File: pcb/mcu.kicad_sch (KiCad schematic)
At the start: 6 parts, among them U5 STM32G0B1RET6

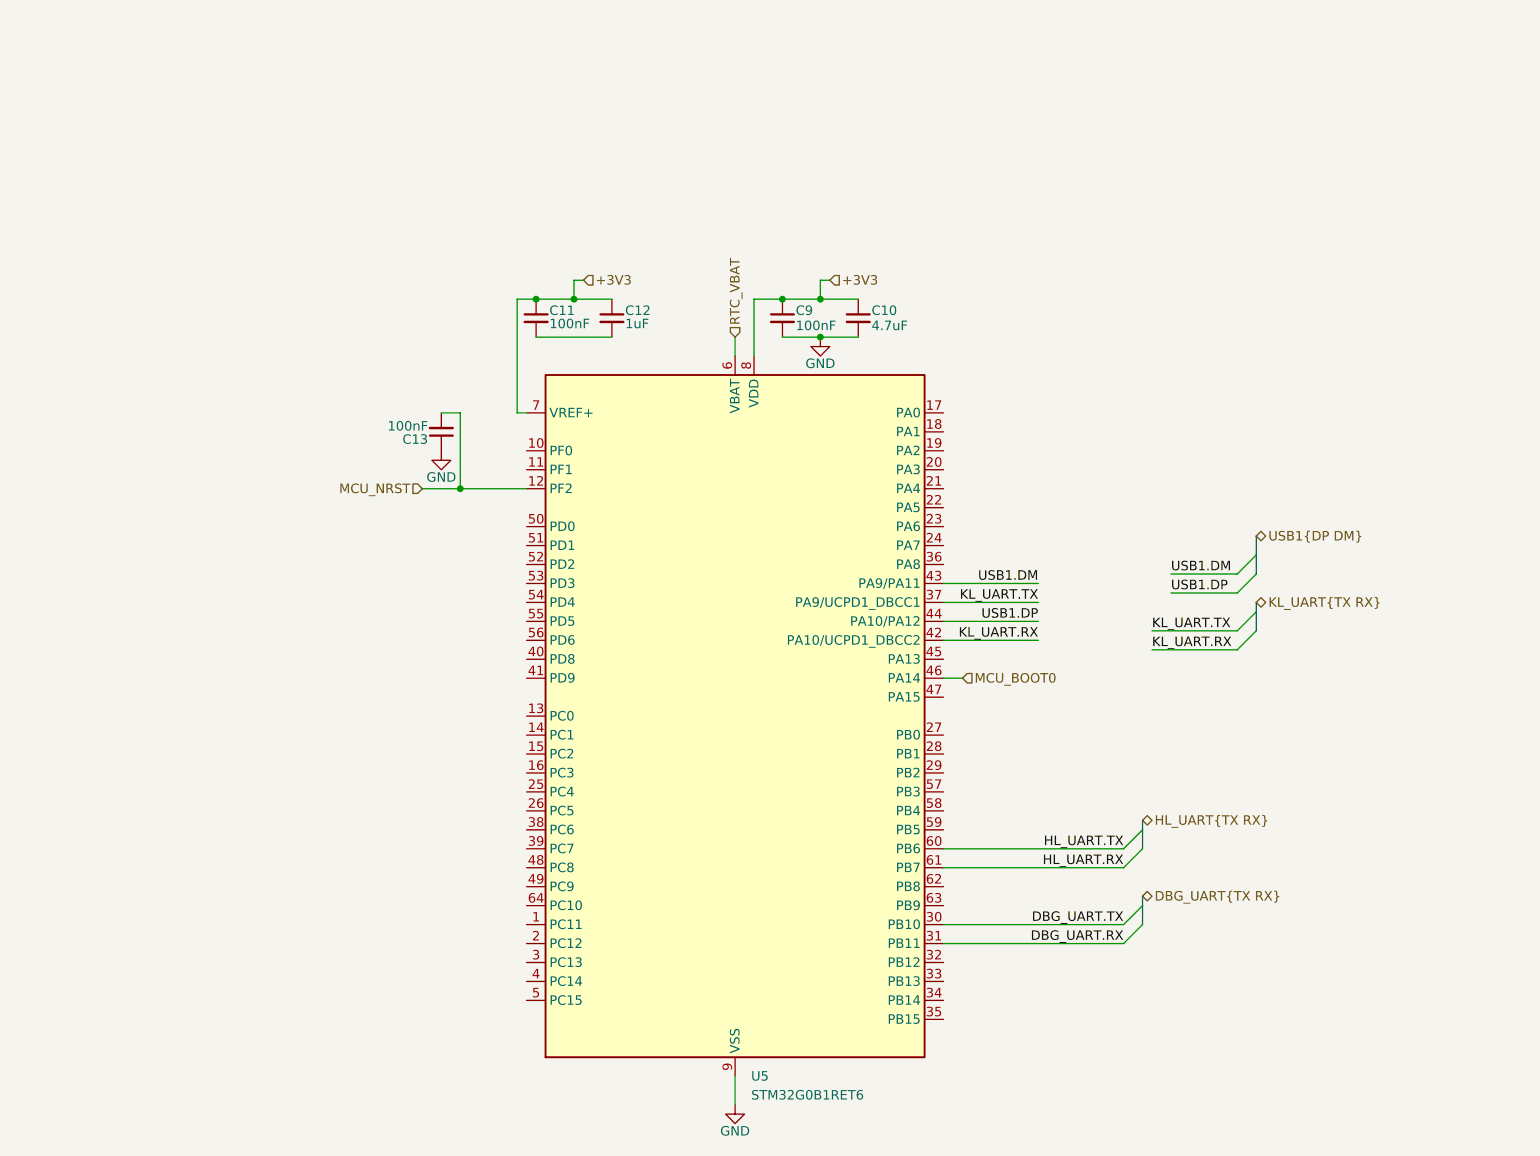
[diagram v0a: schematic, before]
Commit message: pcb gitignore update, netting and mcu pinning
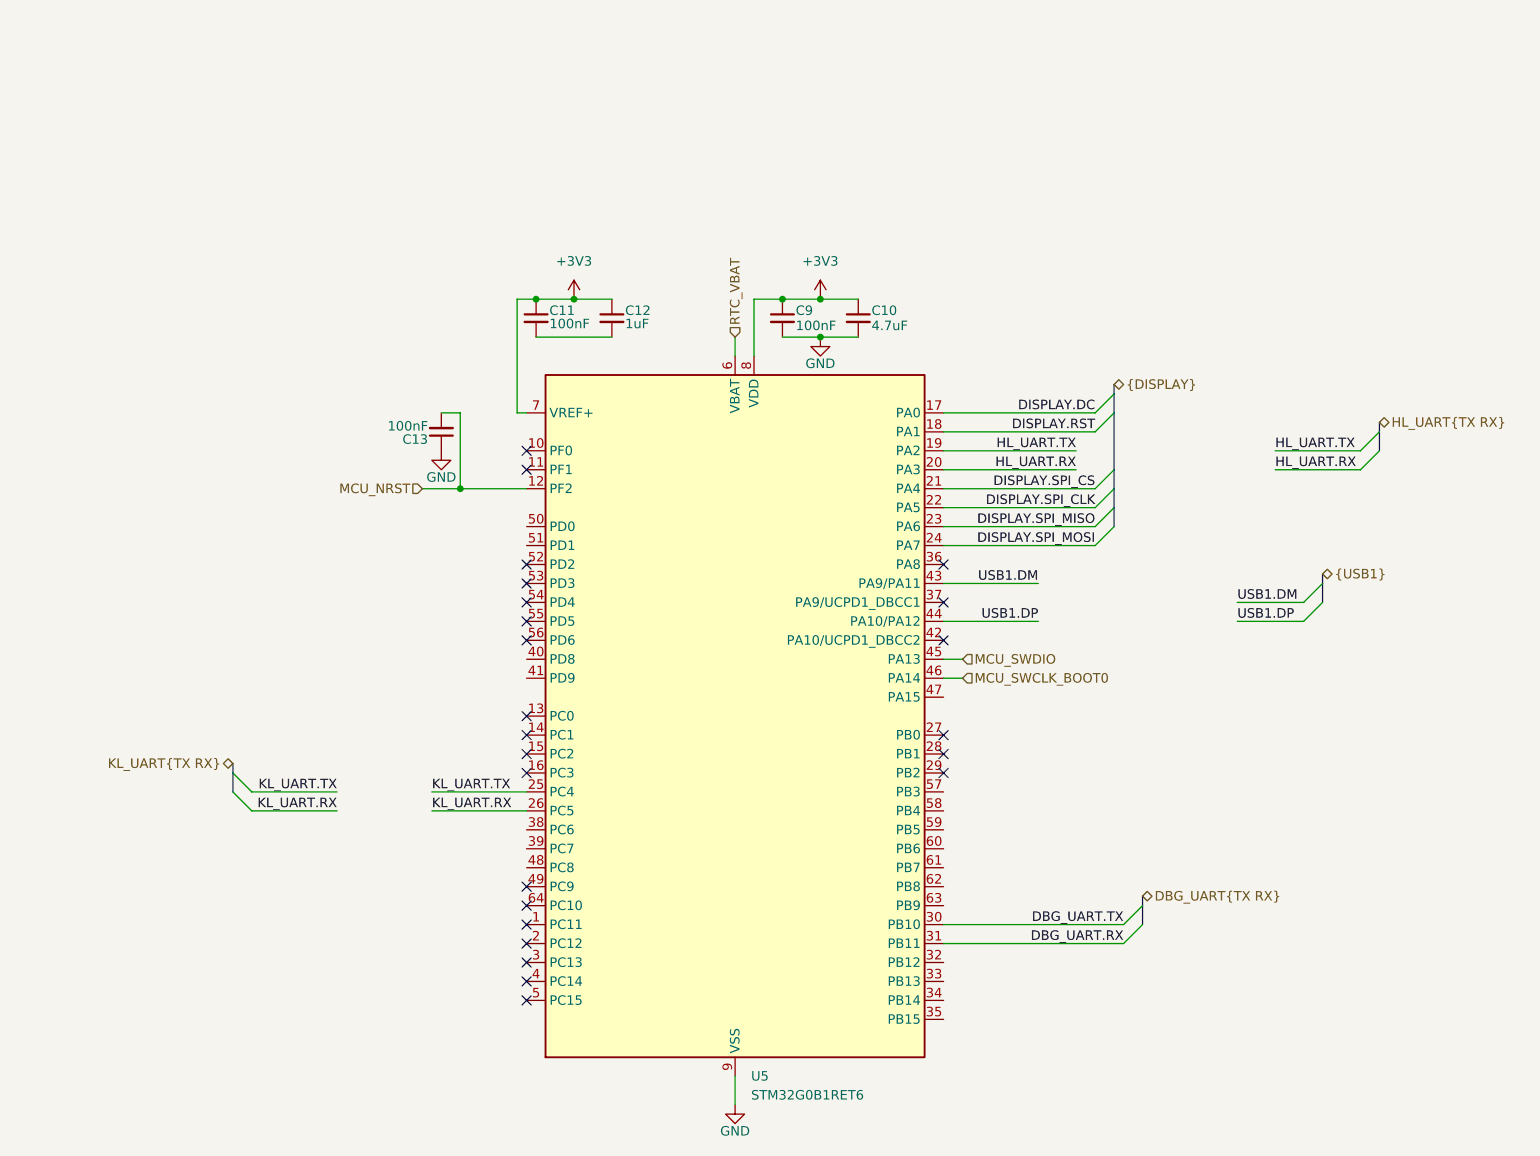
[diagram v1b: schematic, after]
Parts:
- C10, C11, C12, C13, C9: footprint (none) -> Capacitor_SMD:C_0402_1005Metric
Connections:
- net HL_UART.RX: now also U5.20 (PA3); no longer U5.61 (PB7)
- net HL_UART.TX: now also U5.19 (PA2); no longer U5.60 (PB6)
- net KL_UART.RX: now also U5.26 (PC5); no longer U5.42 (PA10/UCPD1_DBCC2)
- net KL_UART.TX: now also U5.25 (PC4); no longer U5.37 (PA9/UCPD1_DBCC1)
- net DISPLAY.DC: now reaches U5.17 (PA0)
- net DISPLAY.RST: now reaches U5.18 (PA1)
- net DISPLAY.SPI_CS: now reaches U5.21 (PA4)
- net DISPLAY.SPI_CLK: now reaches U5.22 (PA5)
- net DISPLAY.SPI_MISO: now reaches U5.23 (PA6)
- net DISPLAY.SPI_MOSI: now reaches U5.24 (PA7)
- net MCU_SWDIO: now reaches U5.45 (PA13)
- net MCU_BOOT0 renamed MCU_SWCLK_BOOT0
- no-connect marks 0 -> 24

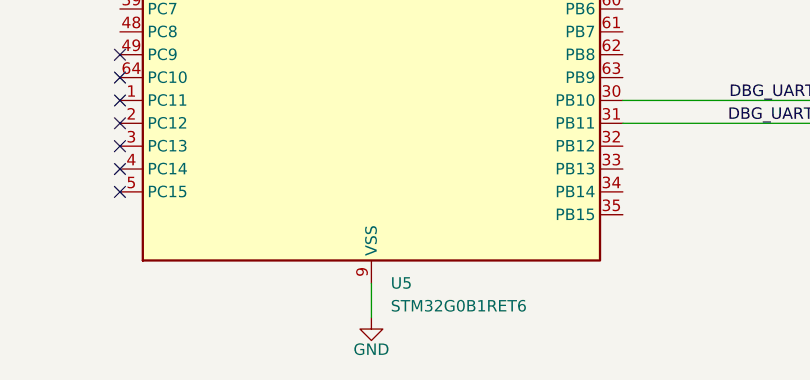
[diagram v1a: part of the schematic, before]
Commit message: add connectors schem
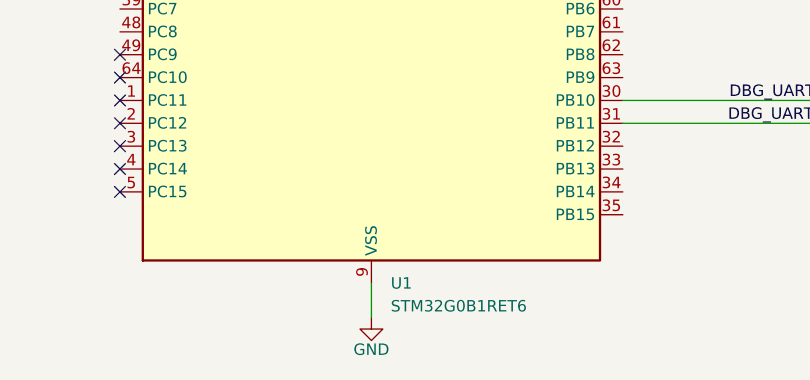
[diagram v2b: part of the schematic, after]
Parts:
- renumbered U5 to U1
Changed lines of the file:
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@@
 		(dnp no)
 		(fields_autoplaced yes)
-		(property "Reference" "U5"
+		(property "Reference" "U1"
 			(at 111.3633 154.94 0)
 			(effects
@@
 		(pin "54"
 		)
+		(instances
+			(project "kh_obd2_interface"
+				(path "/0736e313-8db4-41af-b70d-53af7104d2ca/c18d60e7-bd36-4ea9-b2f1-adbb43a4c5ec"
+					(reference "U1")
+					(unit 1)
+				)
+			)
+		)
 	)

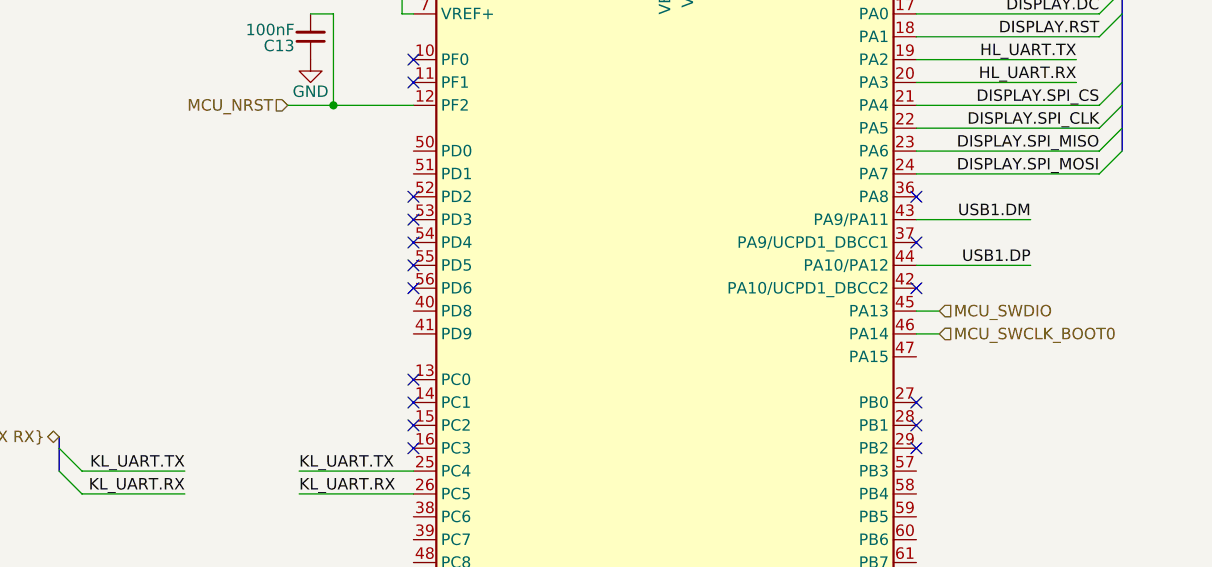
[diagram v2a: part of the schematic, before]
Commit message: add transceivers, routing, drc
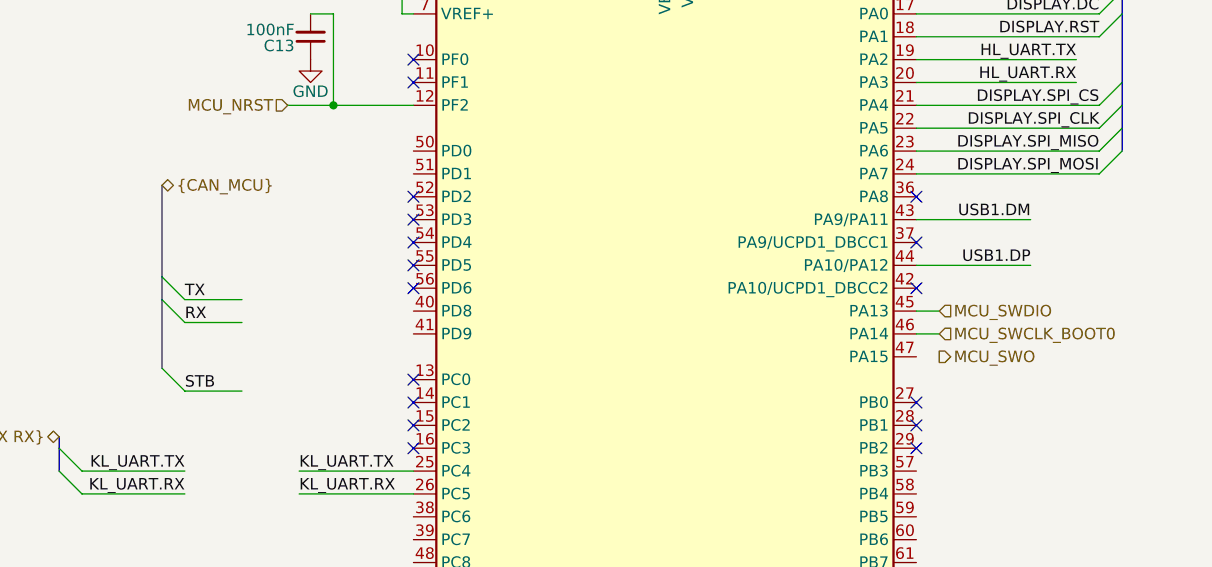
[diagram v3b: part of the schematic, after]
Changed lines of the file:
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@@
+	)
+	(bus_entry
+		(at 53.34 95.25)
+		(size 2.54 2.54)
+		(stroke
+			(width 0)
+			(type default)
+		)
+	)
+	(bus_entry
+		(at 53.34 105.41)
+		(size 2.54 2.54)
+		(stroke
+			(width 0)
+			(type default)
+		)
 	)
 	(bus_entry
@@
 	)
 	(bus_entry
+		(at 53.34 97.79)
+		(size 2.54 2.54)
+		(stroke
+			(width 0)
+			(type default)
+		)
+	)
+	(bus_entry
 		(at 195.58 71.12)
 		(size -2.54 2.54)
@@
 		)
 	)
+	(bus
+		(pts
+			(xy 53.34 85.09) (xy 53.34 95.25)
+		)
+		(stroke
+			(width 0)
+			(type default)
+		)
+	)
 	(wire
 		(pts
@@
 	(wire
 		(pts
+			(xy 55.88 97.79) (xy 62.23 97.79)
+		)
+		(stroke
+			(width 0)
+			(type default)
+		)
+	)
+	(bus
+		(pts
+			(xy 53.34 95.25) (xy 53.34 97.79)
+		)
+		(stroke
+			(width 0)
+			(type default)
+		)
+	)
+	(wire
+		(pts
 			(xy 137.16 76.2) (xy 157.48 76.2)
 		)
@@
 		)
 	)
+	(wire
+		(pts
+			(xy 55.88 107.95) (xy 62.23 107.95)
+		)
+		(stroke
+			(width 0)
+			(type default)
+		)
+	)
 	(bus
 		(pts
@@
 	(bus
 		(pts
+			(xy 53.34 97.79) (xy 53.34 105.41)
+		)
+		(stroke
+			(width 0)
+			(type default)
+		)
+	)
+	(bus
+		(pts
 			(xy 187.96 87.63) (xy 187.96 88.9)
+		)
+		(stroke
+			(width 0)
+			(type default)
+		)
+	)
+	(wire
+		(pts
+			(xy 55.88 100.33) (xy 62.23 100.33)
 		)
 		(stroke
@@
 		)
 	)
+	(label "STB"
+		(at 55.88 107.95 0)
+		(effects
+			(font
+				(size 1.27 1.27)
+			)
+			(justify left bottom)
+		)
+	)
+	(label "TX"
+		(at 55.88 97.79 0)
+		(effects
+			(font
+				(size 1.27 1.27)
+			)
+			(justify left bottom)
+		)
+	)
 	(label "KL_UART.TX"
 		(at 55.88 116.84 180)
@@
 	(label "HL_UART.TX"
 		(at 181.61 71.12 0)
+		(effects
+			(font
+				(size 1.27 1.27)
+			)
+			(justify left bottom)
+		)
+	)
+	(label "RX"
+		(at 55.88 100.33 0)
 		(effects
 			(font
@@
 		)
 	)
+	(hierarchical_label "MCU_SWO"
+		(shape output)
+		(at 139.7 104.14 0)
+		(effects
+			(font
+				(size 1.27 1.27)
+			)
+			(justify left)
+		)
+	)
 	(hierarchical_label "KL_UART{TX RX}"
 		(shape bidirectional)
@@
 		(effects
 			(font
+				(size 1.27 1.27)
+			)
+			(justify left)
+		)
+	)
+	(hierarchical_label "{CAN_MCU}"
+		(shape bidirectional)
+		(at 53.34 85.09 0)
+		(effects
+			(font

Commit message: busses are hard
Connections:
- net RX: now also U1.41 (PD9)
- net TX: now also U1.40 (PD8)
- net HL_UART.RX renamed HLINE.RX
- net HL_UART.TX renamed HLINE.TX
- net KL_UART.RX renamed KLINE.RX
- net KL_UART.TX renamed KLINE.TX
- net USB1.DM renamed DN
- net USB1.DP renamed DP

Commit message: diff skew fixes, routing cleanups
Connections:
- net GND: now also C11.2, C12.2
- no-connect marks 24 -> 38
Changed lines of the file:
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@@
+	)
+	(junction
+		(at 87.63 55.88)
+		(diameter 0)
+		(color 0 0 0 0)
 	)
 	(junction
@@
 	)
 	(no_connect
+		(at 137.16 147.32)
+	)
+	(no_connect
 		(at 81.28 111.76)
 	)
@@
 	)
 	(no_connect
+		(at 81.28 124.46)
+	)
+	(no_connect
 		(at 137.16 96.52)
 	)
 	(no_connect
+		(at 137.16 144.78)
+	)
+	(no_connect
 		(at 81.28 73.66)
 	)
 	(no_connect
+		(at 137.16 142.24)
+	)
+	(no_connect
 		(at 81.28 91.44)
 	)
@@
 	)
 	(no_connect
+		(at 81.28 121.92)
+	)
+	(no_connect
 		(at 81.28 139.7)
 	)
 	(no_connect
+		(at 81.28 127)
+	)
+	(no_connect
+		(at 137.16 124.46)
+	)
+	(no_connect
 		(at 81.28 106.68)
 	)
 	(no_connect
+		(at 137.16 129.54)
+	)
+	(no_connect
+		(at 137.16 139.7)
+	)
+	(no_connect
+		(at 137.16 132.08)
+	)
+	(no_connect
 		(at 81.28 129.54)
 	)
@@
 	)
 	(no_connect
+		(at 137.16 121.92)
+	)
+	(no_connect
 		(at 81.28 86.36)
 	)
@@
 		(at 137.16 109.22)
 	)
+	(no_connect
+		(at 137.16 116.84)
+	)
+	(no_connect
+		(at 137.16 127)
+	)
+	(no_connect
+		(at 137.16 119.38)
+	)
 	(bus_entry
-		(at 180.34 43.18)
+		(at 191.77 64.77)
 		(size -2.54 2.54)
 		(stroke
@@
 	)
 	(bus_entry
-		(at 180.34 50.8)
+		(at 191.77 72.39)
 		(size -2.54 2.54)
 		(stroke
@@
 	)
 	(bus_entry
-		(at 180.34 35.56)
+		(at 191.77 62.23)
 		(size -2.54 2.54)
 		(stroke
@@
 	)
 	(bus_entry
-		(at 180.34 48.26)
+		(at 191.77 69.85)
 		(size -2.54 2.54)
 		(stroke
@@
 	)
 	(bus_entry
-		(at 180.34 33.02)
+		(at 191.77 59.69)
 		(size -2.54 2.54)
 		(stroke
@@
 	)
 	(bus_entry
-		(at 205.74 67.31)
+		(at 191.77 81.28)
 		(size -2.54 2.54)
 		(stroke
@@
 	)
 	(bus_entry
-		(at 205.74 64.77)
+		(at 191.77 78.74)
 		(size -2.54 2.54)
 		(stroke
@@
 	)
 	(bus_entry
-		(at 180.34 45.72)
+		(at 191.77 67.31)
 		(size -2.54 2.54)
 		(stroke
@@
 	(wire
 		(pts
-			(xy 161.29 48.26) (xy 177.8 48.26)
+			(xy 172.72 69.85) (xy 189.23 69.85)
 		)
 		(stroke
@@
 	(wire
 		(pts
-			(xy 161.29 45.72) (xy 177.8 45.72)
+			(xy 172.72 67.31) (xy 189.23 67.31)
 		)
 		(stroke
@@
 	(bus
 		(pts
-			(xy 180.34 45.72) (xy 180.34 48.26)
+			(xy 191.77 67.31) (xy 191.77 69.85)
 		)
 		(stroke
@@
 	(wire
 		(pts
+			(xy 87.63 55.88) (xy 92.71 55.88)
+		)
+		(stroke
+			(width 0)
+			(type default)
+		)
+	)
+	(wire
+		(pts
 			(xy 137.16 99.06) (xy 139.7 99.06)
 		)
@@
 	(wire
 		(pts
-			(xy 82.55 55.88) (xy 92.71 55.88)
+			(xy 82.55 55.88) (xy 87.63 55.88)
 		)
 		(stroke
@@
 	(wire
 		(pts
-			(xy 161.29 38.1) (xy 177.8 38.1)
+			(xy 172.72 64.77) (xy 189.23 64.77)
 		)
 		(stroke
@@
 	(bus
 		(pts
-			(xy 180.34 35.56) (xy 180.34 43.18)
+			(xy 191.77 62.23) (xy 191.77 64.77)
 		)
 		(stroke
@@
 	(bus
 		(pts
-			(xy 205.74 64.77) (xy 205.74 67.31)
+			(xy 191.77 78.74) (xy 191.77 81.28)
 		)
 		(stroke
@@
 	(bus
 		(pts
-			(xy 180.34 31.75) (xy 180.34 33.02)
+			(xy 191.77 58.42) (xy 191.77 59.69)
 		)
 		(stroke
@@
 	(bus
 		(pts
-			(xy 180.34 48.26) (xy 180.34 50.8)
+			(xy 191.77 69.85) (xy 191.77 72.39)
 		)
 		(stroke
@@
 	(wire
 		(pts
-			(xy 161.29 53.34) (xy 177.8 53.34)
-		)
-		(stroke
-			(width 0)
-			(type default)
-		)
-	)
-	(wire
-		(pts
-			(xy 191.77 67.31) (xy 203.2 67.31)
+			(xy 172.72 74.93) (xy 189.23 74.93)
+		)
+		(stroke
+			(width 0)
+			(type default)
+		)
+	)
+	(wire
+		(pts
+			(xy 172.72 81.28) (xy 189.23 81.28)
 		)
 		(stroke
@@
 	(bus
 		(pts
-			(xy 180.34 43.18) (xy 180.34 45.72)
+			(xy 191.77 64.77) (xy 191.77 67.31)
 		)
 		(stroke
@@
 	(wire
 		(pts
-			(xy 161.29 50.8) (xy 177.8 50.8)
+			(xy 172.72 72.39) (xy 189.23 72.39)
 		)
 		(stroke
@@
 	(wire
 		(pts
-			(xy 161.29 35.56) (xy 177.8 35.56)
+			(xy 172.72 62.23) (xy 189.23 62.23)
 		)
 		(stroke
@@
 	(bus
 		(pts
-			(xy 180.34 33.02) (xy 180.34 35.56)
-		)
-		(stroke
-			(width 0)
-			(type default)
-		)
-	)
-	(wire
-		(pts
-			(xy 191.77 69.85) (xy 203.2 69.85)
+			(xy 191.77 59.69) (xy 191.77 62.23)
+		)
+		(stroke
+			(width 0)
+			(type default)
+		)
+	)
+	(wire
+		(pts
+			(xy 172.72 83.82) (xy 189.23 83.82)
 		)
 		(stroke
@@
 	(bus
 		(pts
-			(xy 205.74 63.5) (xy 205.74 64.77)
+			(xy 191.77 77.47) (xy 191.77 78.74)
 		)
 		(stroke
@@
 	)
 	(label "DISPLAY.RST"
-		(at 161.29 38.1 0)
+		(at 172.72 64.77 0)
 		(effects
 			(font
@@
 	)
 	(label "DISPLAY.SPI_CS"
-		(at 161.29 45.72 0)
+		(at 172.72 67.31 0)
 		(effects
 			(font
@@
 	)
 	(label "HLINE.RX"
-		(at 191.77 69.85 0)
+		(at 172.72 83.82 0)
 		(effects
 			(font
@@
 	)
 	(label "DISPLAY.SPI_MISO"
-		(at 161.29 50.8 0)
+		(at 172.72 72.39 0)
 		(effects
 			(font
@@
 	)
 	(label "DISPLAY.SPI_MOSI"
-		(at 161.29 53.34 0)
+		(at 172.72 74.93 0)
 		(effects
 			(font
@@
 	)
 	(label "DISPLAY.DC"
-		(at 161.29 35.56 0)
+		(at 172.72 62.23 0)
 		(effects
 			(font
@@
 	)
 	(label "HLINE.TX"
-		(at 191.77 67.31 0)
+		(at 172.72 81.28 0)
 		(effects
 			(font
@@
 	)
 	(label "DISPLAY.SPI_CLK"
-		(at 161.29 48.26 0)
+		(at 172.72 69.85 0)
 		(effects
 			(font
@@
 	(hierarchical_label "DISPLAY{DISPLAY}"
 		(shape bidirectional)
-		(at 180.34 31.75 180)
+		(at 191.77 58.42 180)
 		(effects
 			(font
@@
 	(hierarchical_label "HLINE{UART}"
 		(shape bidirectional)
-		(at 205.74 63.5 180)
+		(at 191.77 77.47 180)
 		(effects
 			(font
@@
 					(unit 1)
 				)
+			)
+		)
+	)
+	(symbol
+		(lib_id "power:GND")
+		(at 87.63 55.88 0)
+		(unit 1)
+		(exclude_from_sim no)
+		(in_bom yes)
+		(on_board yes)
+		(dnp no)
+		(property "Reference" "#PWR041"
+			(at 87.63 62.23 0)
+			(effects
+				(font
+					(size 1.27 1.27)
+				)
+				(hide yes)
+			)
+		)
+		(property "Value" "GND"
+			(at 87.63 59.436 0)
+			(effects
+				(font
+					(size 1.27 1.27)
+				)
+			)
+		)
+		(property "Footprint" ""
+			(at 87.63 55.88 0)
+			(effects
+				(font
+					(size 1.27 1.27)
+				)
+				(hide yes)
+			)
+		)
+		(property "Datasheet" ""
+			(at 87.63 55.88 0)
+			(effects
+				(font
+					(size 1.27 1.27)
+				)
+				(hide yes)
+			)
+		)
+		(property "Description" "Power symbol creates a global label with name \"GND\" , ground"
+			(at 87.63 55.88 0)
+			(effects
+				(font
+					(size 1.27 1.27)
+				)
+				(hide yes)
+			)
+		)
+		(pin "1"
+		)
+		(instances
+			(project "kh_obd2_interface"
+				(path "/0736e313-8db4-41af-b70d-53af7104d2ca/c18d60e7-bd36-4ea9-b2f1-adbb43a4c5ec"
+					(reference "#PWR041")
+					(unit 1)
+				)
